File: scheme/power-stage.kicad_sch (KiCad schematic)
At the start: 19 parts, among them U9 CSD95472Q5MC

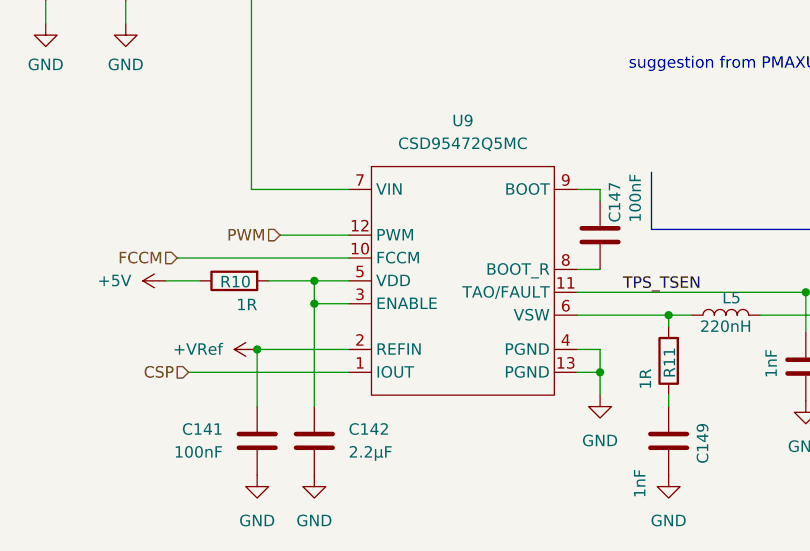
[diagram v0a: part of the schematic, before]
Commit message: Updated schematics with correct cap rating
We upgraded certain capacitors to a higher nF rating and have changed the schematic to reflect it so the BOM can be generated accurately.
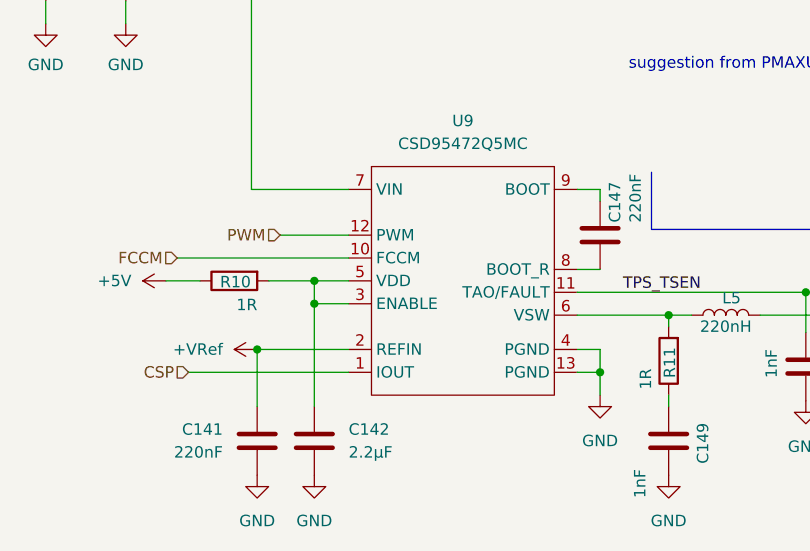
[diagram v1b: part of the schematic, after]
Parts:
- C141, C147: value 100nF -> 220nF; OrderNr 399-C0805C104K5RACTUCT-ND -> 399-C0805C224K5RACTUTR-ND
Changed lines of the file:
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@@
 			)
 		)
-		(property "Value" "100nF"
+		(property "Value" "220nF"
 			(at 150.622 95.758 90)
 			(effects
@@
 			)
 		)
-		(property "OrderNr" "399-C0805C104K5RACTUCT-ND"
+		(property "OrderNr" "399-C0805C224K5RACTUTR-ND"
 			(at 146.685 97.155 0)
 			(effects
@@
 			)
 		)
-		(property "Value" "100nF"
+		(property "Value" "220nF"
 			(at 104.775 121.2849 0)
 			(effects
@@
 			)
 		)
-		(property "OrderNr" "399-C0805C104K5RACTUCT-ND"
+		(property "OrderNr" "399-C0805C224K5RACTUTR-ND"
 			(at 108.585 120.015 0)
 			(effects
